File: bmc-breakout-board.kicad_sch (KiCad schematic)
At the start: 5 parts

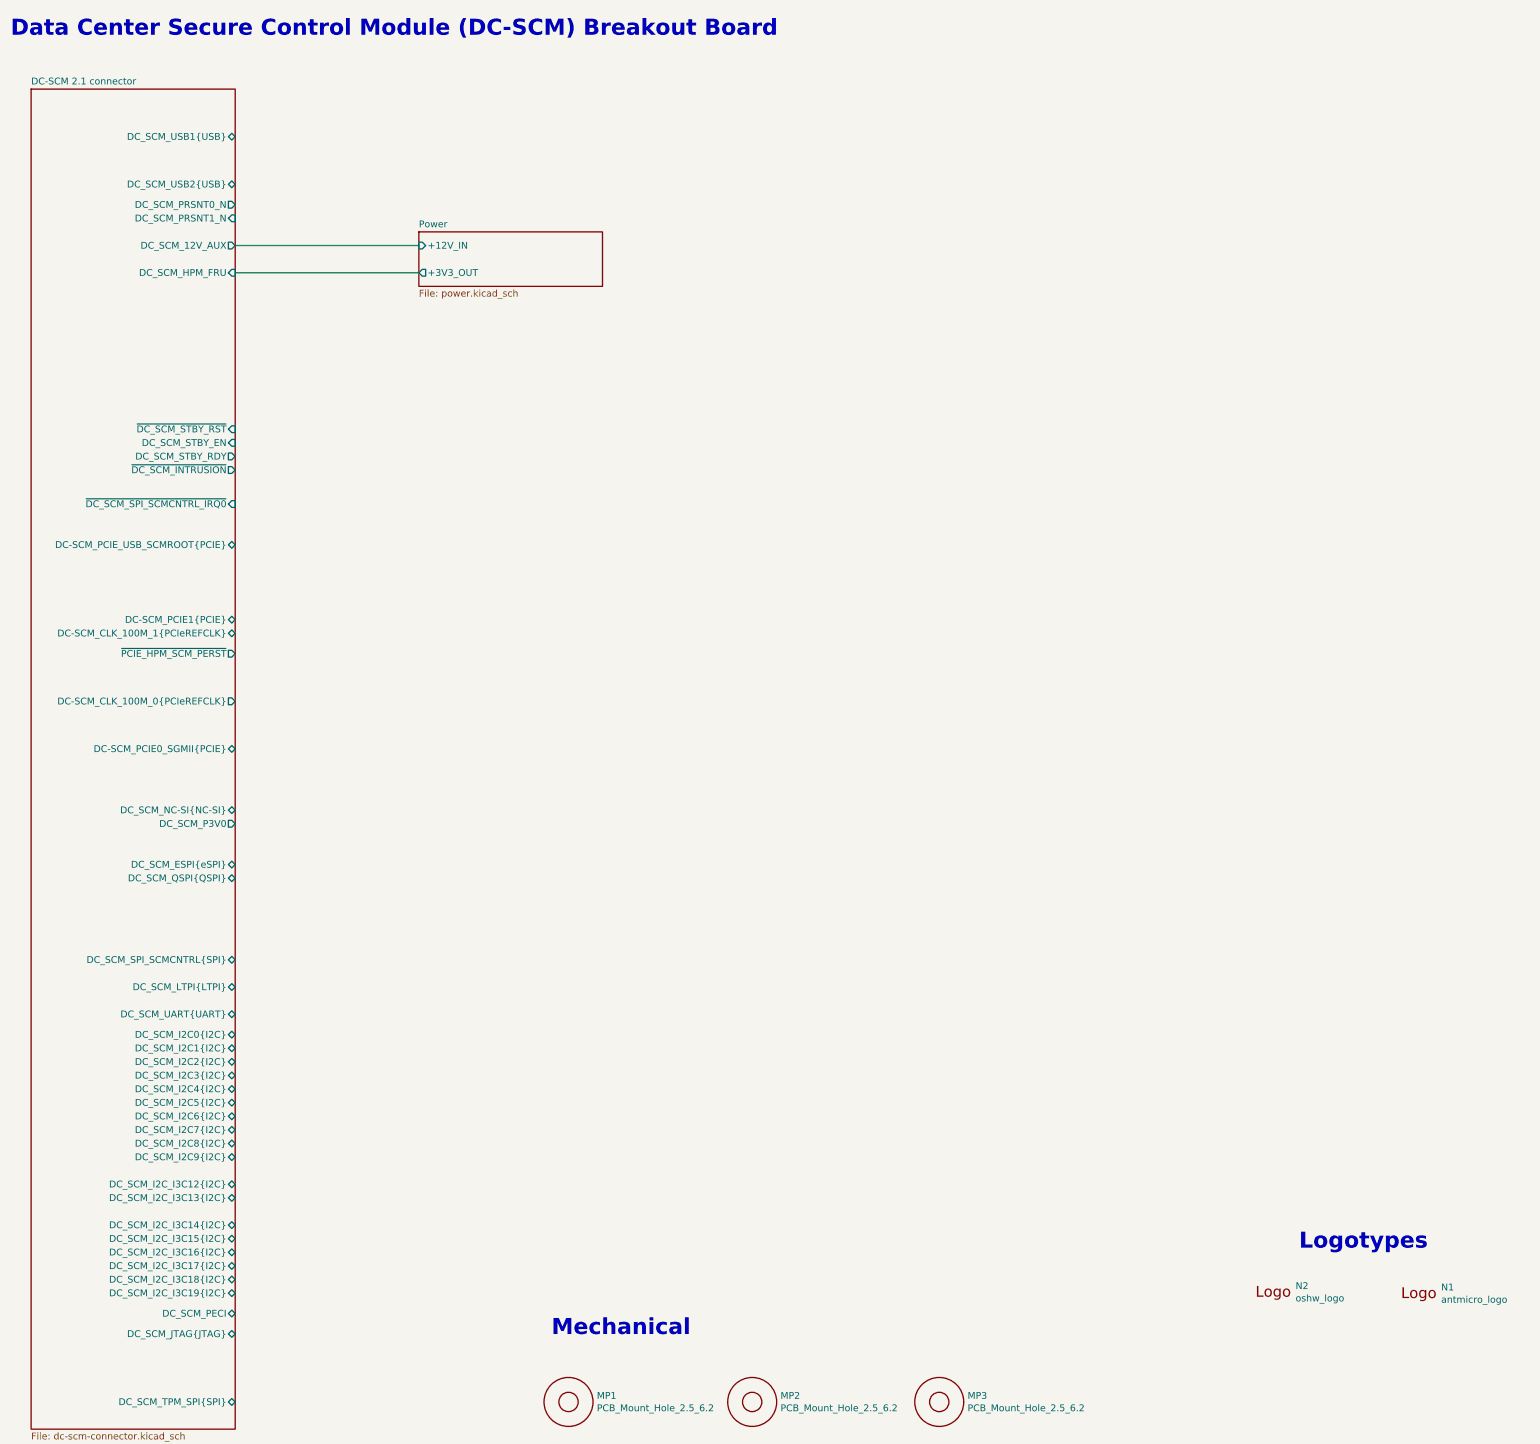
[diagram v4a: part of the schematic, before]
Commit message: [#92504] Add 12V power to DCM-SCM
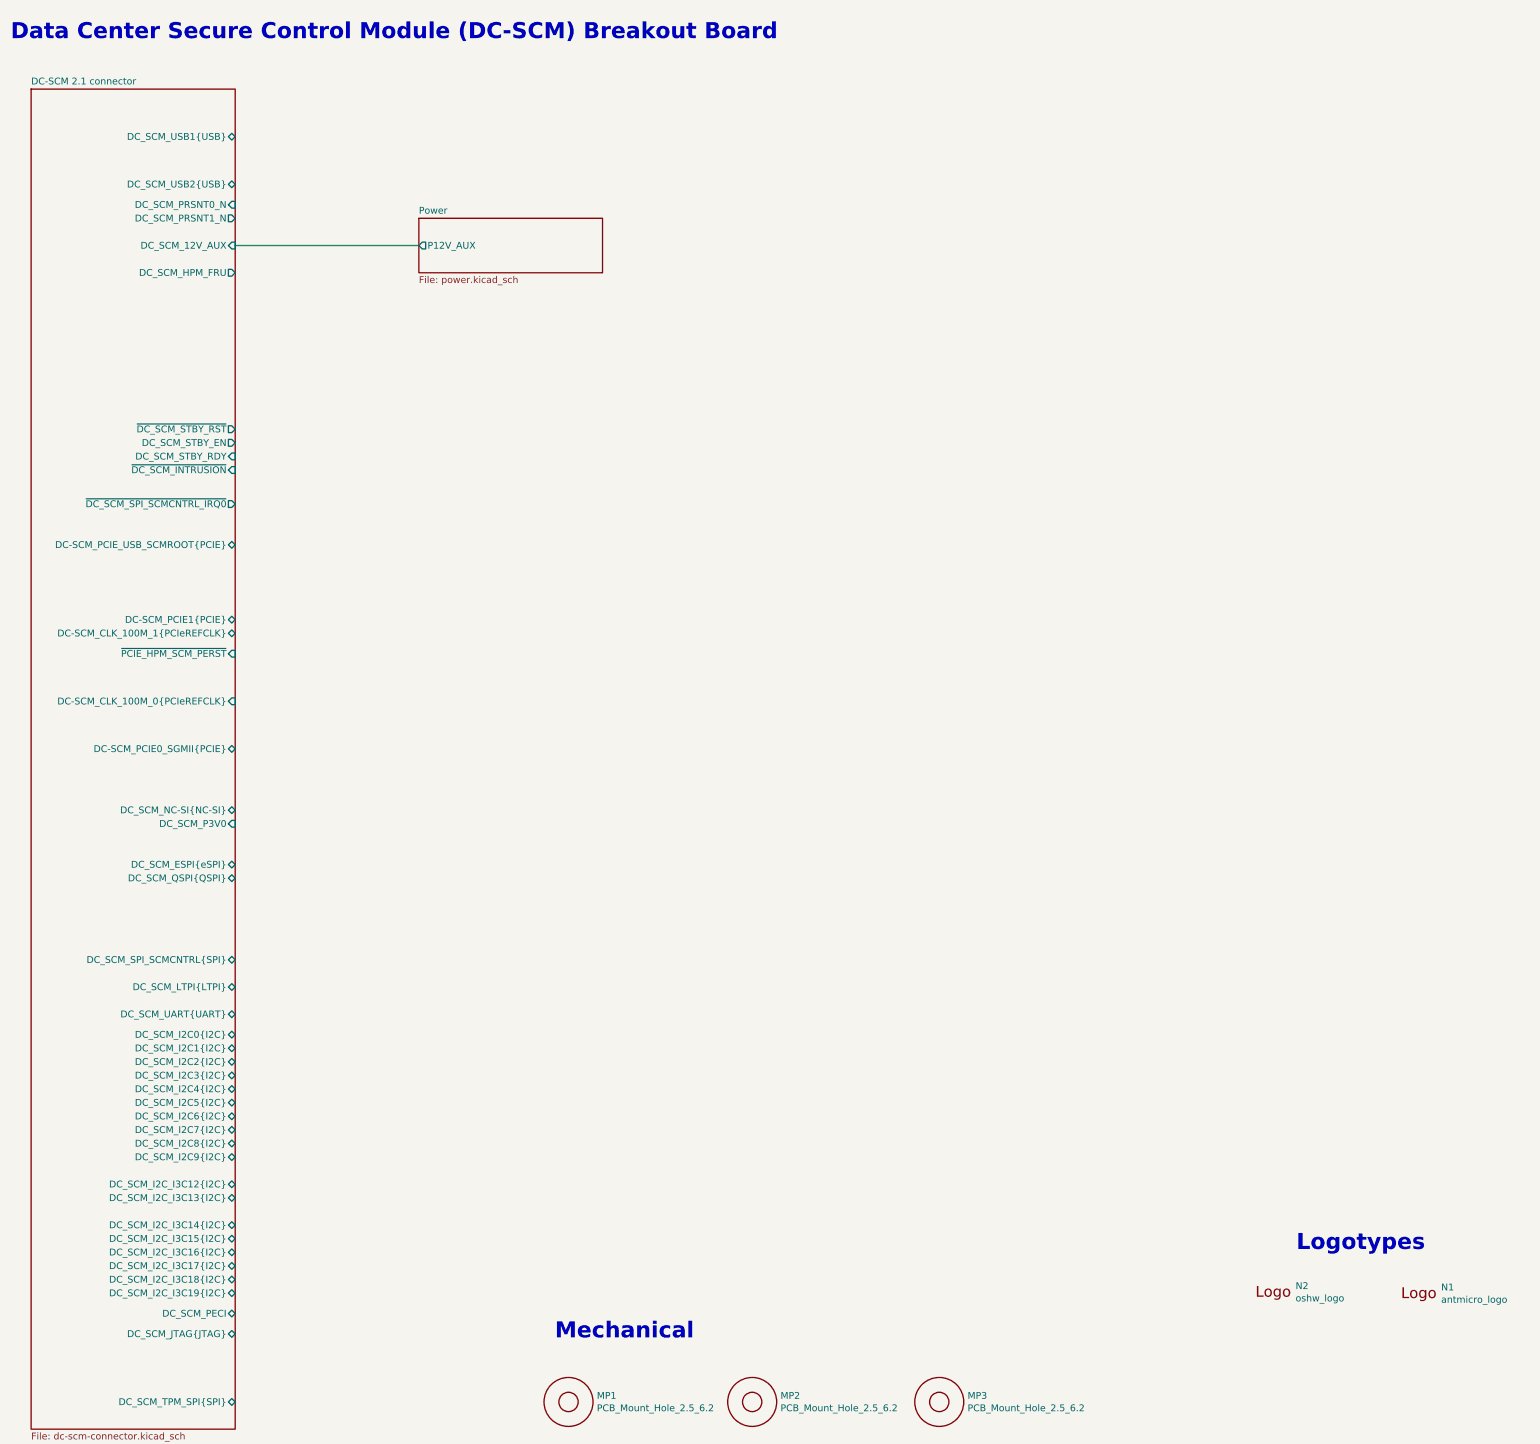
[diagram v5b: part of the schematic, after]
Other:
- sheet Power ports: added P12V_AUX; removed +12V_IN, +3V3_OUT
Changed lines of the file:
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@@
 	(text "Logotypes"
 		(exclude_from_sim no)
-		(at 255.778 247.396 0)
+		(at 255.27 247.65 0)
 		(effects
 			(font
@@
 	(text "Mechanical"
 		(exclude_from_sim no)
-		(at 116.205 263.525 0)
+		(at 116.84 264.16 0)
 		(effects
 			(font
@@
 	(text "Data Center Secure Control Module (DC-SCM) Breakout Board"
 		(exclude_from_sim no)
-		(at 15.24 20.955 0)
+		(at 15.24 21.59 0)
 		(effects
 			(font
@@
 		)
 	)
-	(wire
-		(pts
-			(xy 57.15 64.77) (xy 91.44 64.77)
-		)
-		(stroke
-			(width 0)
-			(type default)
-		)
-	)
 	(image
 		(at 288.925 272.415)
@@
 	)
 	(sheet
-		(at 91.44 57.15)
+		(at 91.44 54.61)
 		(size 34.29 10.16)
 		(exclude_from_sim no)
@@
 		)
 		(property "Sheetname" "Power"
-			(at 91.44 56.4384 0)
+			(at 91.44 53.8984 0)
 			(effects
 				(font
@@
 		)
 		(property "Sheetfile" "power.kicad_sch"
-			(at 91.44 67.8946 0)
+			(at 91.44 65.3546 0)
 			(effects
 				(font
@@
 			)
 		)
-		(pin "+12V_IN" input
+		(pin "P12V_AUX" output
 			(at 91.44 59.69 180)
 			(effects
@@
 			)
 		)
-		(pin "+3V3_OUT" output
-			(at 91.44 64.77 180)
-			(effects
-				(font
-					(size 1.27 1.27)
-				)
-				(justify left)
-			)
-		)
 		(instances
 			(project "bmc-breakout-board"
@@
 			)
 		)
-		(pin "DC_SCM_PRSNT0_N" output
+		(pin "DC_SCM_PRSNT0_N" input
 			(at 57.15 52.07 0)
 			(effects
@@
 			)
 		)
-		(pin "DC_SCM_12V_AUX" output
+		(pin "DC_SCM_12V_AUX" input
 			(at 57.15 59.69 0)
 			(effects
@@
 			)
 		)
-		(pin "DC_SCM_P3V0" output
+		(pin "DC_SCM_P3V0" input
 			(at 57.15 167.64 0)
 			(effects
@@
 			)
 		)
-		(pin "DC_SCM_PRSNT1_N" input
+		(pin "DC_SCM_PRSNT1_N" output
 			(at 57.15 54.61 0)
 			(effects
@@
 			)
 		)
-		(pin "DC_SCM_STBY_EN" input
+		(pin "DC_SCM_STBY_EN" output
 			(at 57.15 96.52 0)
 			(effects
@@
 			)
 		)
-		(pin "DC_SCM_STBY_RDY" output
+		(pin "DC_SCM_STBY_RDY" input
 			(at 57.15 99.06 0)
 			(effects
@@
 			)
 		)
-		(pin "DC_SCM_HPM_FRU" input
+		(pin "DC_SCM_HPM_FRU" output
 			(at 57.15 64.77 0)
 			(effects
@@
 			)
 		)
-		(pin "~{DC_SCM_SPI_SCMCNTRL_IRQ0}" input
+		(pin "~{DC_SCM_SPI_SCMCNTRL_IRQ0}" output
 			(at 57.15 107.95 0)
 			(effects
@@
 			)
 		)
-		(pin "DC-SCM_CLK_100M_0{PCIeREFCLK}" output
+		(pin "DC-SCM_CLK_100M_0{PCIeREFCLK}" input
 			(at 57.15 144.78 0)
 			(effects
@@
 			)
 		)
-		(pin "~{DC_SCM_INTRUSION}" output
+		(pin "~{DC_SCM_INTRUSION}" input
 			(at 57.15 101.6 0)
 			(effects
@@
 			)
 		)
-		(pin "~{DC_SCM_STBY_RST}" input
+		(pin "~{DC_SCM_STBY_RST}" output
 			(at 57.15 93.98 0)
 			(effects
@@
 			)
 		)
-		(pin "~{PCIE_HPM_SCM_PERST}" output
+		(pin "~{PCIE_HPM_SCM_PERST}" input
 			(at 57.15 135.89 0)
 			(effects

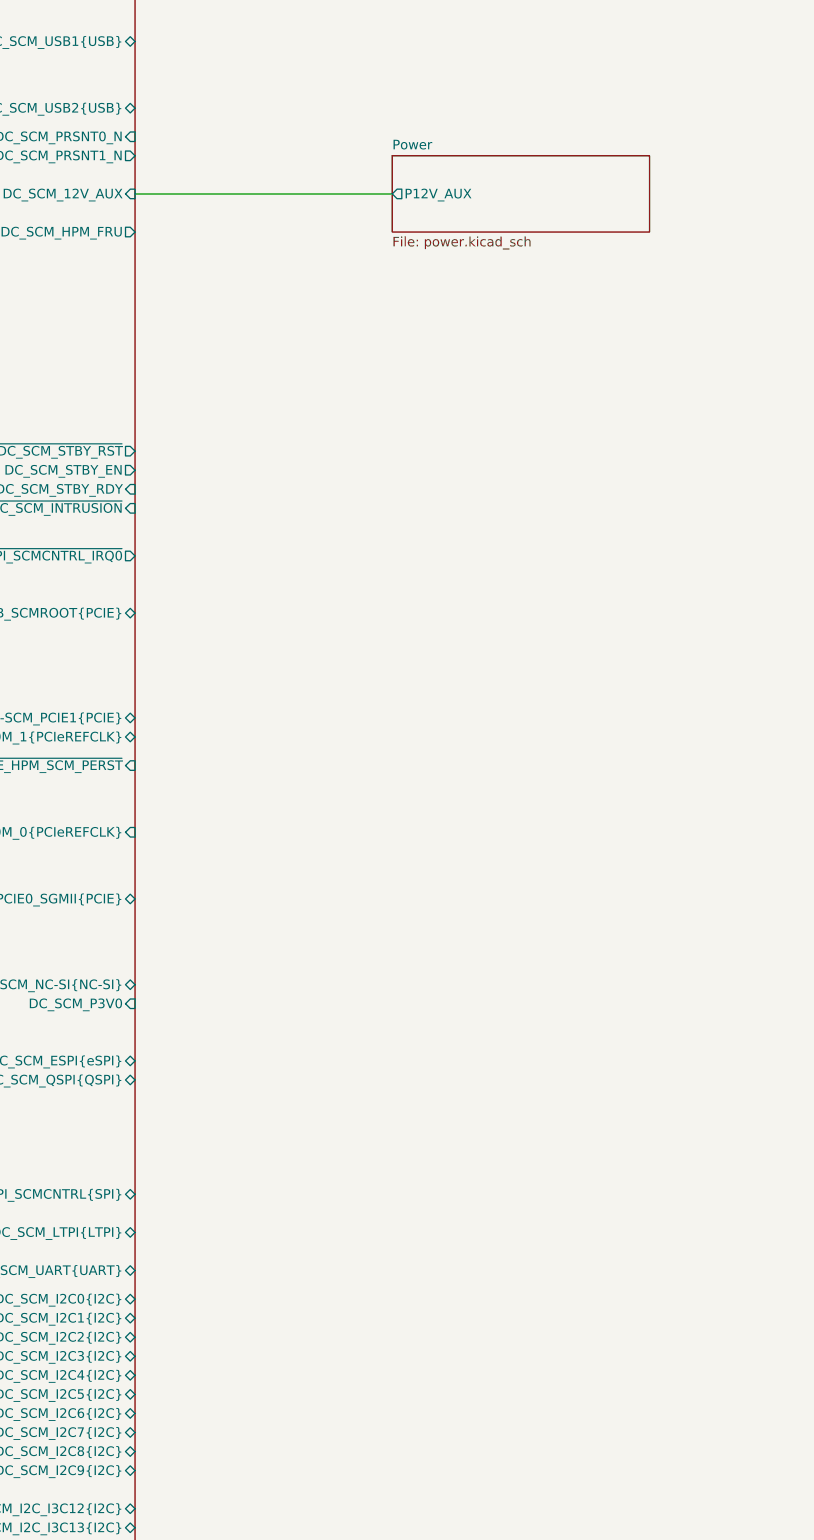
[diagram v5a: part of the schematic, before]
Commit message: [#92504] Add 3V3 DCDC converter
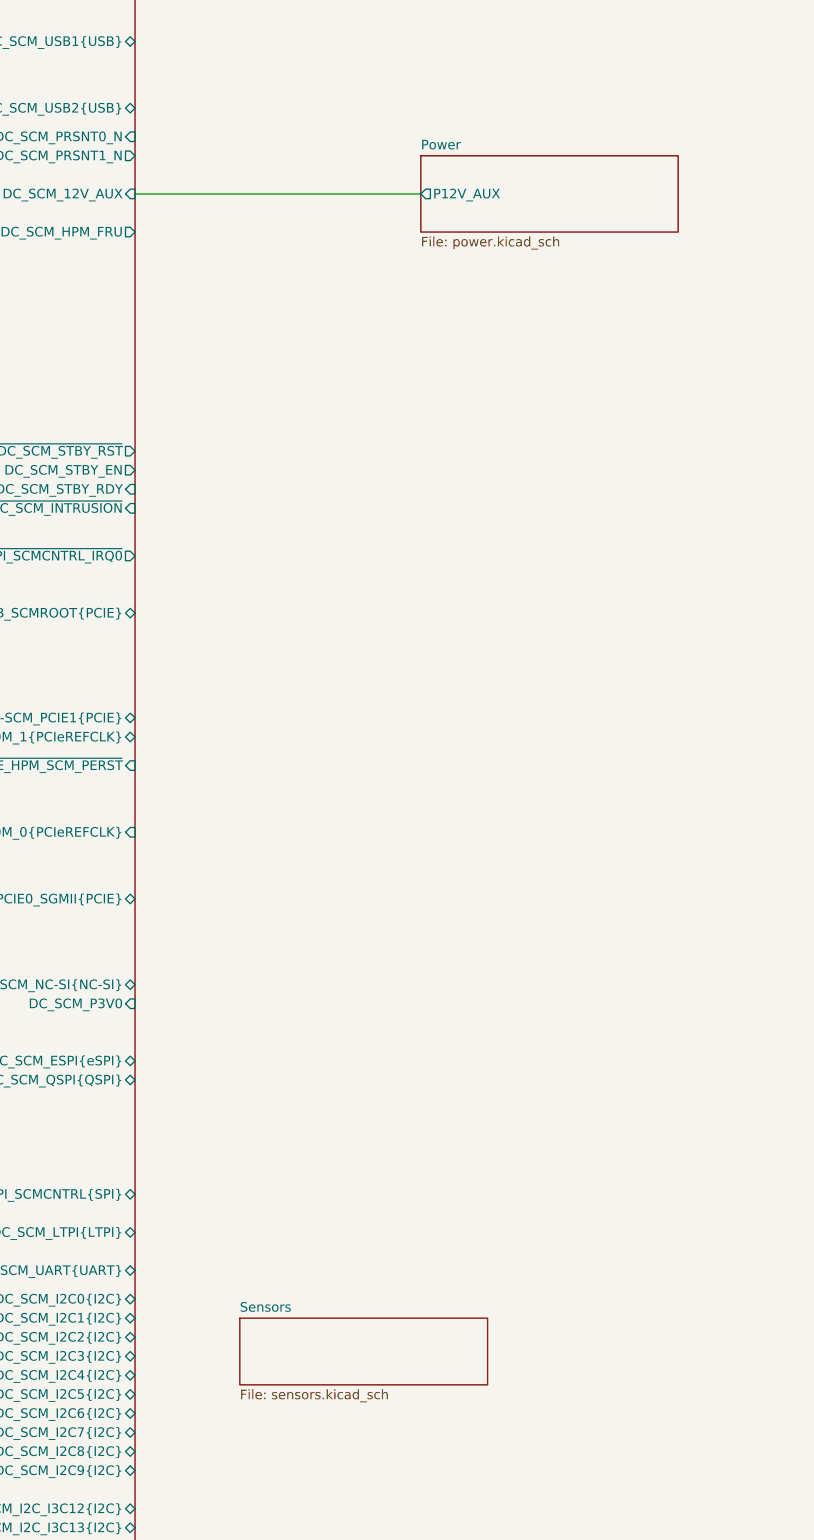
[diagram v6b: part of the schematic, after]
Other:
- added sheet Sensors (sensors.kicad_sch)
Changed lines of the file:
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@@
 	(wire
 		(pts
-			(xy 57.15 59.69) (xy 91.44 59.69)
+			(xy 57.15 59.69) (xy 95.25 59.69)
 		)
 		(stroke
@@
 	)
 	(sheet
-		(at 91.44 54.61)
+		(at 95.25 54.61)
 		(size 34.29 10.16)
 		(exclude_from_sim no)
@@
 		)
 		(property "Sheetname" "Power"
-			(at 91.44 53.8984 0)
+			(at 95.25 53.8984 0)
 			(effects
 				(font
@@
 		)
 		(property "Sheetfile" "power.kicad_sch"
-			(at 91.44 65.3546 0)
+			(at 95.25 65.3546 0)
 			(effects
 				(font
@@
 		)
 		(pin "P12V_AUX" output
-			(at 91.44 59.69 180)
+			(at 95.25 59.69 180)
 			(effects
 				(font
@@
 				)
 			)
+		)
+	)
+	(sheet
+		(at 71.12 209.55)
+		(size 33.02 8.89)
+		(exclude_from_sim no)
+		(in_bom yes)
+		(on_board yes)
+		(dnp no)
+		(fields_autoplaced yes)
+		(stroke
+			(width 0.1524)
+			(type solid)
+		)
+		(fill
+			(color 0 0 0 0.0000)
+		)
+		(property "Sheetname" "Sensors"
+			(at 71.12 208.8384 0)
+			(effects
+				(font
+					(size 1.27 1.27)
+				)
+				(justify left bottom)
+			)
+		)
+		(property "Sheetfile" "sensors.kicad_sch"
+			(at 71.12 219.0246 0)
+			(effects
+				(font
+					(size 1.27 1.27)
+				)
+				(justify left top)
+			)
+		)
+		(instances
+			(project "bmc-breakout-board"
+				(path "/5d67ef28-5805-4f87-b722-2926dabf7f6e"
+					(page "4")
+				)
+			)
